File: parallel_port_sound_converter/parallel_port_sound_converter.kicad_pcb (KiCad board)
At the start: 2 copper layers, 39.4 x 36.8 mm, 16 parts, among them J1 DB25_Male, J2 DB25_Female, U1 LM78L05_TO92, U2 ATtiny2313A-PU

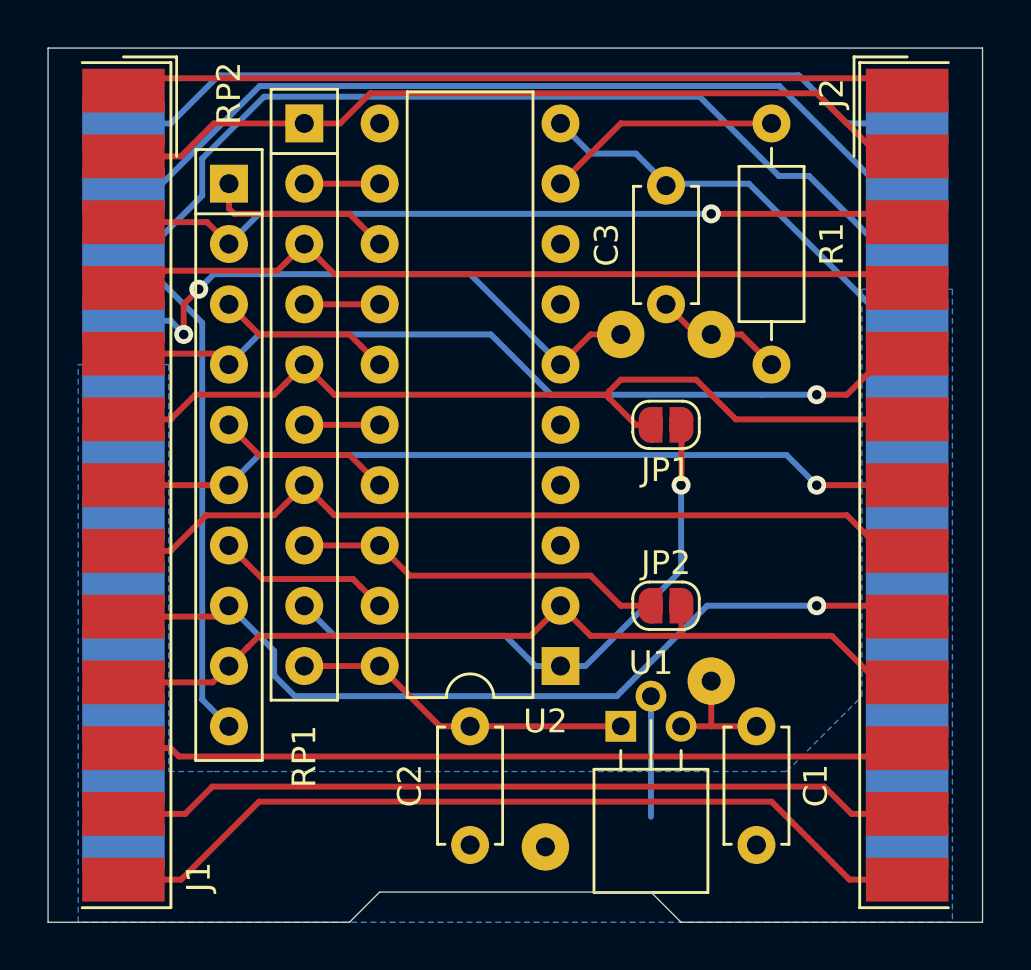
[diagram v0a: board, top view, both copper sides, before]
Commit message: switch to ATtiny24
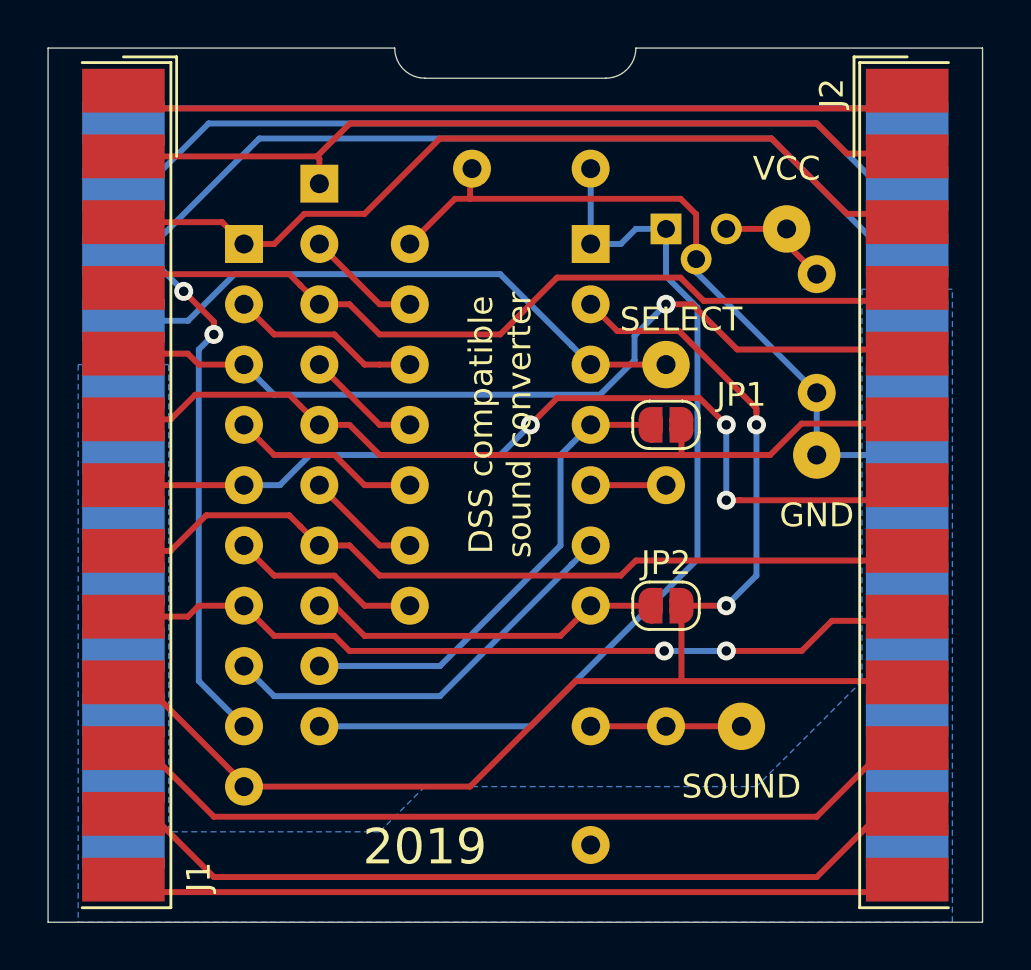
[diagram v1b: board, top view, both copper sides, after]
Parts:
- C1, C2, C3, R1, RP1, RP2, U1: moved to B.Cu
- U2: value ATtiny2313A-PU -> ATtiny24-20PU; footprint Package_DIP:DIP-20_W7.62mm -> Package_DIP:DIP-14_W7.62mm; moved to B.Cu
- moved C2 24.0 mm to (108.6, 75.6), turned to 180 degrees
- moved U1 21.0 mm to (111.8, 78.1)
- moved TP1 20.1 mm to (118.1, 87.6)
- moved TP2 19.3 mm to (116.8, 78.1)
- moved C1 19.2 mm to (118.1, 80.0)
- moved C3 18.1 mm to (108.6, 99.1), turned to 270 degrees
- moved U2 17.8 mm to (108.6, 78.7)
- moved TP4 16.6 mm to (114.9, 99.1)
- moved R1 15.9 mm to (111.8, 99.1)
- moved RP1 2.62 mm to (97.2, 76.2)
- moved RP2 2.62 mm to (94.0, 78.7)
- moved TP3 2.29 mm to (111.8, 83.8)
- turned JP1 to 180 degrees
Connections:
- RP2 pad 1: /MCU_D1 -> /D1
- RP2 pad 10: /C2 -> /S6_MISO
- RP2 pad 2: /D1 -> /MCU_D1
- RP2 pad 3: /MCU_D3 -> /D3
- RP2 pad 4: /D3 -> /MCU_D3
- RP2 pad 5: /MCU_D5_MOSI -> /D5_MOSI
- RP2 pad 6: /D5_MOSI -> /MCU_D5_MOSI
- RP2 pad 7: /MCU_D7_SCK -> /D7_SCK
- RP2 pad 8: /D7_SCK -> /MCU_D7_SCK
- RP2 pad 9: /S6_MISO -> /C2
- U2 pad 1: /RESET -> +5V
- U2 pad 10: GND -> /MCU_D3
- U2 pad 11: Net-(U2-Pad11) -> /MCU_D2
- U2 pad 12: /MCU_D0 -> /MCU_D1
- U2 pad 13: /MCU_D1 -> /MCU_D0
- U2 pad 14: /MCU_D2 -> GND
- U2 pad 3: Net-(U2-Pad3) -> /C3
- U2 pad 4: Net-(U2-Pad4) -> /RESET
- U2 pad 5: Net-(U2-Pad5) -> /PWM_OUT
- U2 pad 6: /C3 -> /MCU_D7_SCK
- U2 pad 7: Net-(U2-Pad7) -> /MCU_D6_MISO
- U2 pad 8: Net-(U2-Pad8) -> /MCU_D5_MOSI
- U2 pad 9: /PWM_OUT -> /MCU_D4_RESET
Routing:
- net +5V: track 14.4 -> 39.9 mm
- net /S6_MISO: track 35.7 -> 59.5 mm, vias 0 -> 2
- net /MCU_D7_SCK: track 7.40 -> 17.8 mm
- net GND: track 23.1 -> 30.4 mm
- net /PWM_OUT: track 9.94 -> 3.18 mm
- net /RESET: track 24.7 -> 20.4 mm, vias 1 -> 0
- net /D5_MOSI: track 34.1 -> 37.8 mm, vias 1 -> 3
- net /D7_SCK: track 36.6 -> 33.9 mm, vias 1 -> 2
- net /C2: track 60.9 -> 58.2 mm, vias 0 -> 2
- net /S4: track 35.6 -> 33.3 mm
- net /D1: track 34.2 -> 35.9 mm, vias 1 -> 0
- net /D4_RESET: track 38.0 -> 36.3 mm
- net /MCU_D2: track 3.17 -> 4.86 mm
- net /MCU_D0: track 3.17 -> 4.86 mm
- net /MCU_D4_RESET: track 3.17 -> 4.86 mm
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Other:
- outline, holes or cut-outs redrawn
